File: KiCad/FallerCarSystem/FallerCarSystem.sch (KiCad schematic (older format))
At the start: 32 parts, among them M1 Motor_DC, Q1 BS170F, SW1 SW_DIP_x01, SW2 SW_Reed, U1 PIC12F675-ISN, U2 LT3080xST, U3 MCP1525-TT

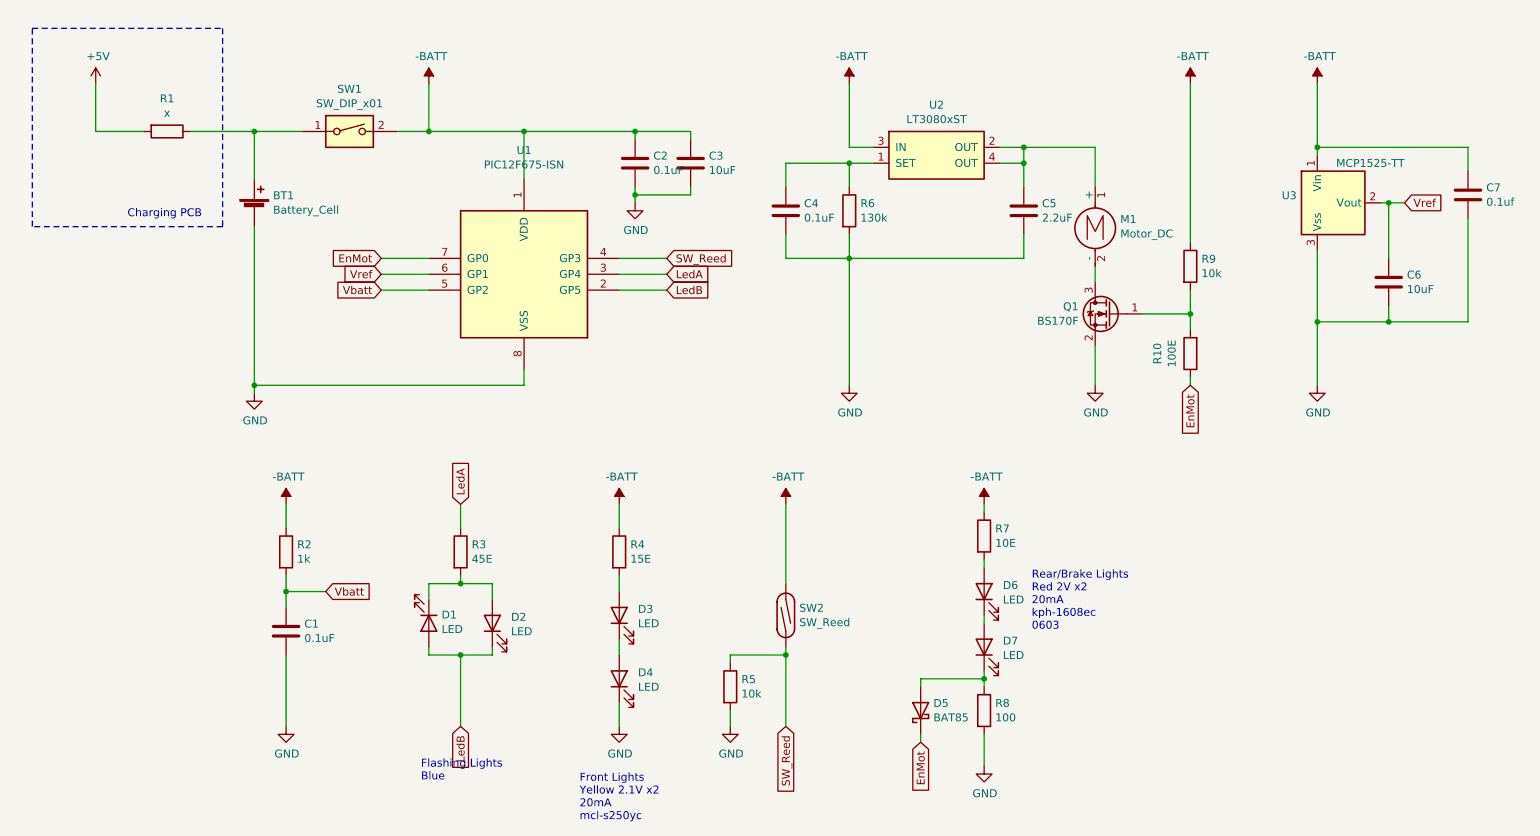
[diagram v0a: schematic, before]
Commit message: jumped to new PIC: 16F-LF-15324. Updated schematic.
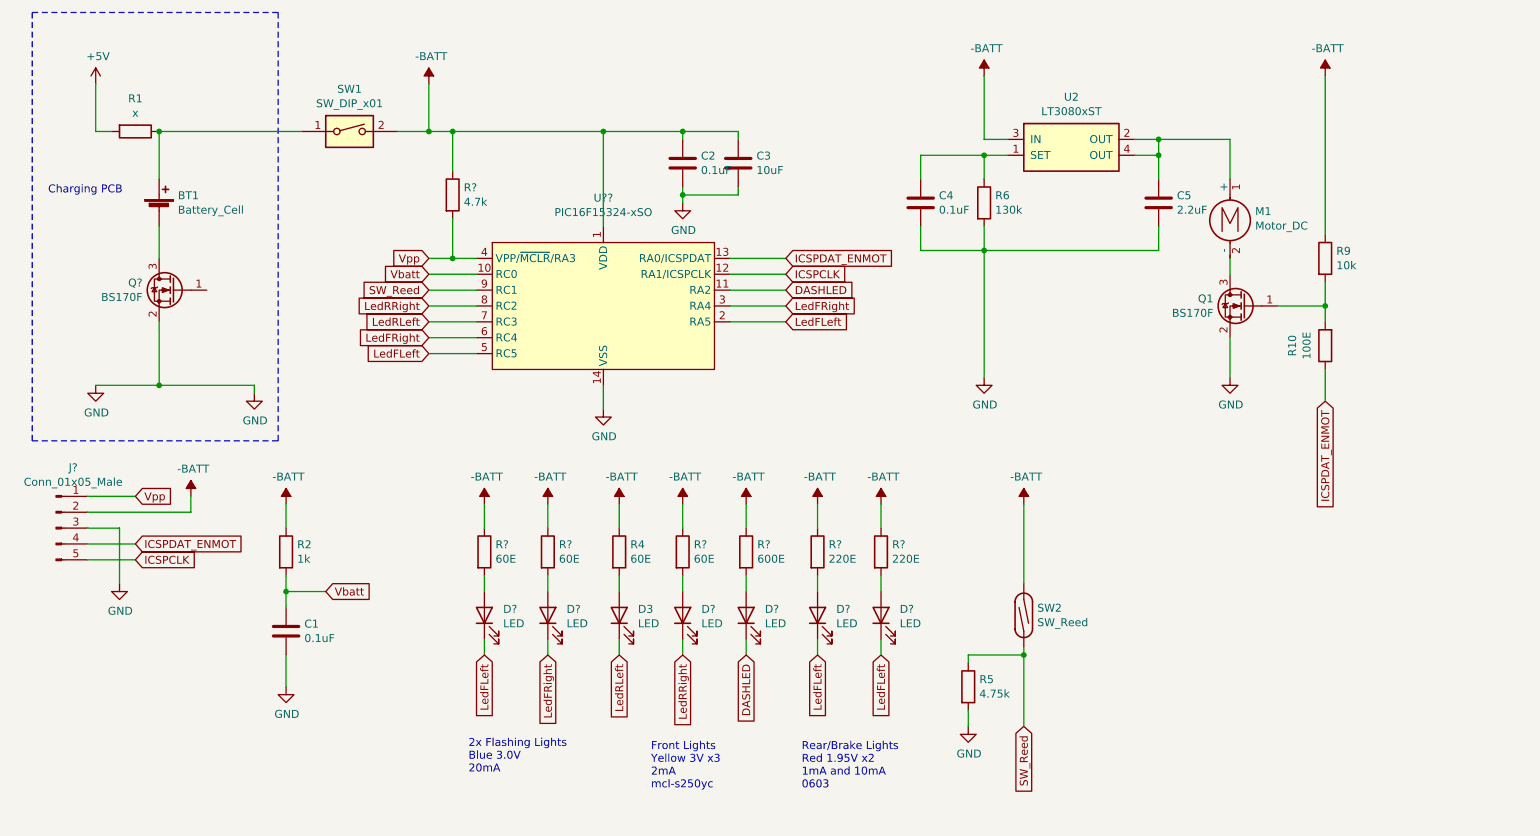
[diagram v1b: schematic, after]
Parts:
- removed C6: 10uF, symbol Device:C
- removed C7: 0.1uf, symbol Device:C
- removed D1, D2, D4, D6, D7: LED, symbol Device:LED
- removed D5: BAT85, Diode_THT:D_DO-35_SOD27_P7.62mm_Horizontal, symbol Diode:BAT85
- removed R3: 45E, symbol Device:R
- removed R7: 10E, symbol Device:R
- removed R8: 100, symbol Device:R
- removed U1: PIC12F675-ISN, Package_DIP:DIP-8_W7.62mm, symbol MCU_Microchip_PIC12:PIC12F675-ISN
- removed U3: MCP1525-TT, Package_TO_SOT_SMD:SOT-23, symbol Reference_Voltage:MCP1525-TT
- added D? (x6): LED, symbol Device:LED
- added J?: Conn_01x05_Male, symbol Connector:Conn_01x05_Male
- added Q?: BS170F, Package_TO_SOT_SMD:SOT-23, symbol Transistor_FET:BS170F
- added R?: 4.7k, symbol Device:R
- added R? (x3): 60E, symbol Device:R
- added R?: 600E, symbol Device:R
- added R? (x2): 220E, symbol Device:R
- added U??: PIC16F15324-xSO, Package_SO:SOIC-14W_7.5x17.9mm_P1.27mm, symbol MCU_Microchip_PIC16:PIC16F15324-xSO
- R4: value 15E -> 60E
- R5: value 10k -> 4.75k
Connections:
- net -BATT: now also J?.2 (Pin_2), R?.1, R?.1, R?.1, R?.1, R?.1, R?.1, R?.1, U??.1 (VDD)
- net GND: now also J?.3 (Pin_3), Q?.2 (S), U??.14 (VSS); no longer BT1.2 (-)
- net SW_Reed: now also U??.9 (RC1)
- net Vbatt: now also U??.10 (RC0)
- net LedRLeft: now reaches D3.1 (K)
- net LedRLeft: now also U??.7 (RC3)
- net EnMot renamed ICSPDAT_ENMOT
- net ICSPDAT_ENMOT: now also J?.4 (Pin_4), U??.13 (RA0/ICSPDAT)
- new net: BT1.2 (-), Q?.3 (D)
- new net: D?.2 (A), R?.2 (x6)
- new net DASHLED: D?.1 (K), U??.11 (RA2)
- new net ICSPCLK: J?.5 (Pin_5), U??.12 (RA1/ICSPCLK)
- new net LedFLeft: D?.1 (K), D?.1 (K), D?.1 (K), U??.2 (RA5), U??.5 (RC5)
- new net LedFRight: D?.1 (K), U??.3 (RA4), U??.6 (RC4)
- new net LedRRight: D?.1 (K), U??.8 (RC2)
- new net Vpp: J?.1 (Pin_1), R?.2, U??.4 (VPP/~MCLR~/RA3)
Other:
- note added: "2x Flashing Lights\nBlue 3.0V\n20mA"
- note added: "Front Lights\nYellow 3V x3\n2mA\nmcl-s250yc"
- note added: "Rear/Brake Lights\nRed 1.95V x2\n1mA and 10mA\n0603"
- note removed: "Flashing Lights\nBlue"
- note removed: "Front Lights\nYellow 2.1V x2\n20mA\nmcl-s250yc"
- note removed: "Rear/Brake Lights\nRed 2V x2\n20mA\nkph-1608ec\n0603"
- moved on the sheet: BT1, C2, C3, C4, C5, M1, Q1, R1, R10, R5, R6, R9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

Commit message: First proto version faller car system done. To do: - develop PCB with charger on it etc - Front led lights in flash mode may go deeper off
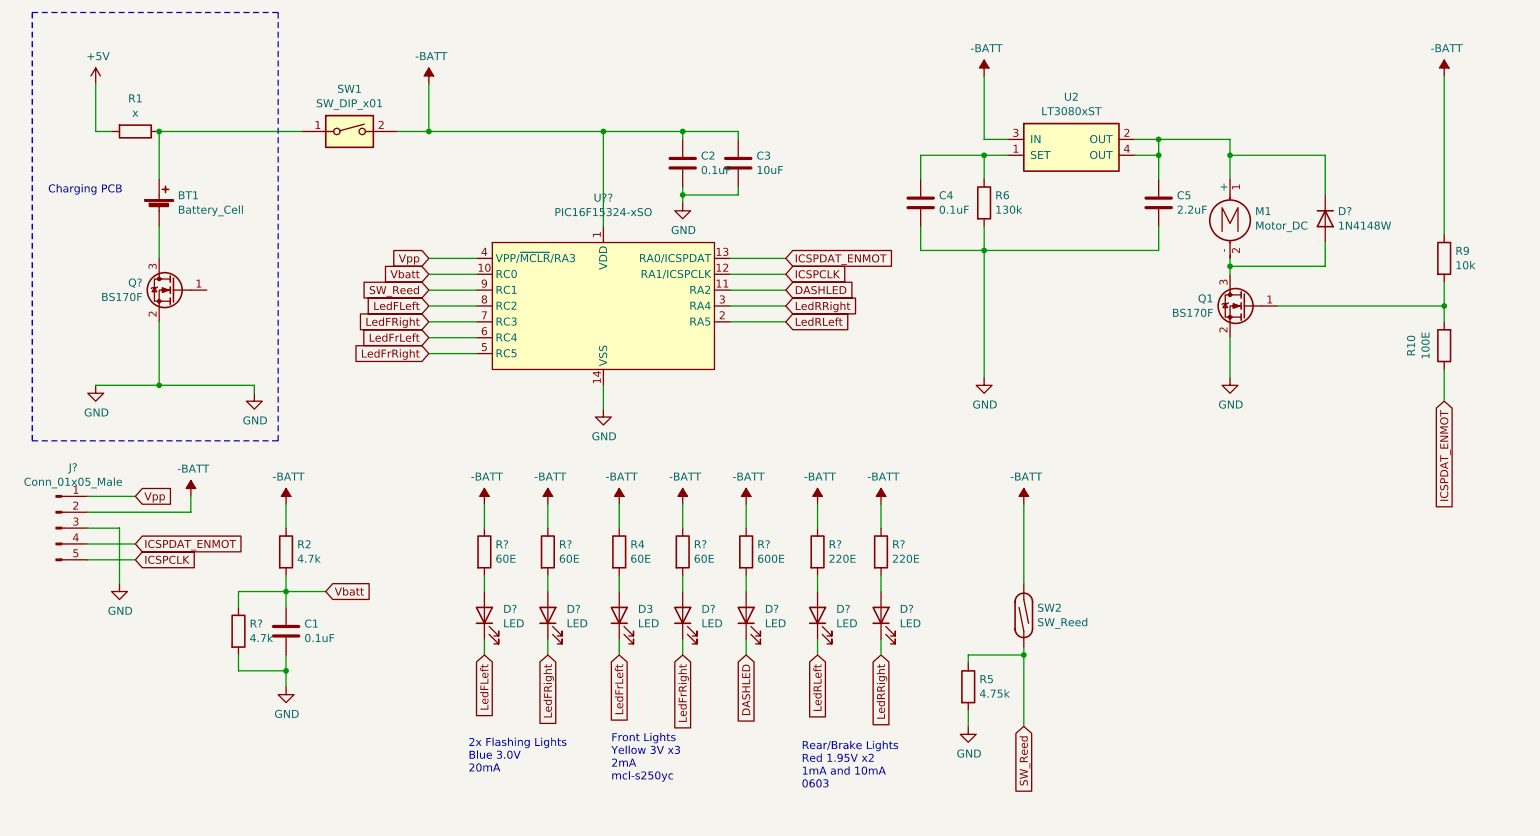
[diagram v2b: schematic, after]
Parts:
- removed R?: 4.7k, symbol Device:R
- added D?: 1N4148W, Diode_SMD:D_SOD-123, symbol Diode:1N4148W
- added R?: 4.7k, symbol Device:R
- R2: value 1k -> 4.7k
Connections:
- net GND: now also R?.2
- net LedFLeft: now also U??.8 (RC2); no longer D?.1 (K), D?.1 (K), U??.2 (RA5), U??.5 (RC5)
- net LedFRight: now also U??.7 (RC3); no longer U??.3 (RA4), U??.6 (RC4)
- net LedRLeft: now also D?.1 (K), U??.2 (RA5); no longer D3.1 (K), U??.7 (RC3)
- net LedRRight: now also D?.1 (K), U??.3 (RA4); no longer D?.1 (K), U??.8 (RC2)
- net Vbatt: now also R?.1
- net at C5.1, M1.1 (+), U2.2 (OUT)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: now also D?.1 (K)
- net at M1.2 (-), Q1.3 (D): now also D?.2 (A)
- new net LedFrLeft: D3.1 (K), U??.6 (RC4)
- new net LedFrRight: D?.1 (K), U??.5 (RC5)
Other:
- moved on the sheet: R10, R9
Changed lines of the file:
@@
 P 2400 4150
 F 0 "R2" H 2470 4196 50  0000 L CNN
-F 1 "1k" H 2470 4105 50  0000 L CNN
+F 1 "4.7k" H 2470 4105 50  0000 L CNN
 F 2 "" V 2330 4150 50  0001 C CNN
 F 3 "~" H 2400 4150 50  0001 C CNN
@@
 L Device:R R10
 U 1 1 639E8742
-P 8950 2850
-F 0 "R10" V 9157 2850 50  0000 C CNN
-F 1 "100E" V 9066 2850 50  0000 C CNN
-F 2 "" V 8880 2850 50  0001 C CNN
-F 3 "~" H 8950 2850 50  0001 C CNN
-	1    8950 2850
+P 9700 2850
+F 0 "R10" V 9907 2850 50  0000 C CNN
+F 1 "100E" V 9816 2850 50  0000 C CNN
+F 2 "" V 9630 2850 50  0001 C CNN
+F 3 "~" H 9700 2850 50  0001 C CNN
+	1    9700 2850
 	-1   0    0    1
 $EndComp
@@
 L Device:R R9
 U 1 1 639EBB86
-P 8950 2300
-F 0 "R9" H 9020 2346 50  0000 L CNN
-F 1 "10k" H 9020 2255 50  0000 L CNN
-F 2 "" V 8880 2300 50  0001 C CNN
-F 3 "~" H 8950 2300 50  0001 C CNN
-	1    8950 2300
+P 9700 2300
+F 0 "R9" H 9770 2346 50  0000 L CNN
+F 1 "10k" H 9770 2255 50  0000 L CNN
+F 2 "" V 9630 2300 50  0001 C CNN
+F 3 "~" H 9700 2300 50  0001 C CNN
+	1    9700 2300
 	1    0    0    -1
 $EndComp
@@
 Wire Wire Line
 	4500 4300 4500 4400
-Text Notes 4700 5650 0    50   ~ 0
-Front Lights\nYellow 3V x3\n2mA\nmcl-s250yc
 Wire Wire Line
 	6800 1550 6950 1550
@@
 Connection ~ 7900 1550
 Wire Wire Line
-	8350 2400 8350 2300
-Wire Wire Line
-	8350 1800 8350 1550
+	8350 2400 8350 2350
+Wire Wire Line
+	8350 1800 8350 1650
 $Comp
 L power:-BATT #PWR010
@@
 L power:-BATT #PWR016
 U 1 1 63ADE5C4
-P 8950 1150
-F 0 "#PWR016" H 8950 1000 50  0001 C CNN
-F 1 "-BATT" H 8965 1323 50  0000 C CNN
-F 2 "" H 8950 1150 50  0001 C CNN
-F 3 "" H 8950 1150 50  0001 C CNN
-	1    8950 1150
-	1    0    0    -1
-$EndComp
-Wire Wire Line
-	8950 1150 8950 2150
-Wire Wire Line
-	8950 2450 8950 2600
-Wire Wire Line
-	8950 2600 8650 2600
-Wire Wire Line
-	8950 2600 8950 2700
-Connection ~ 8950 2600
+P 9700 1150
+F 0 "#PWR016" H 9700 1000 50  0001 C CNN
+F 1 "-BATT" H 9715 1323 50  0000 C CNN
+F 2 "" H 9700 1150 50  0001 C CNN
+F 3 "" H 9700 1150 50  0001 C CNN
+	1    9700 1150
+	1    0    0    -1
+$EndComp
+Wire Wire Line
+	9700 1150 9700 2150
+Wire Wire Line
+	9700 2450 9700 2600
+Wire Wire Line
+	9700 2600 9700 2700
+Connection ~ 9700 2600
 Wire Wire Line
 	8350 2800 8350 3050
@@
 	1    0    0    -1
 $EndComp
-Wire Wire Line
-	3300 1500 3450 1500
 Connection ~ 3300 1500
 Wire Wire Line
@@
 Text GLabel 3300 2300 0    50   Input ~ 0
 Vpp
-Wire Wire Line
-	3300 2300 3450 2300
-$Comp
-L Device:R R?
-U 1 1 63A04FA2
-P 3450 1900
-F 0 "R?" H 3520 1946 50  0000 L CNN
-F 1 "4.7k" H 3520 1855 50  0000 L CNN
-F 2 "" V 3380 1900 50  0001 C CNN
-F 3 "~" H 3450 1900 50  0001 C CNN
-	1    3450 1900
-	1    0    0    -1
-$EndComp
-Wire Wire Line
-	3450 2050 3450 2300
-Connection ~ 3450 2300
-Wire Wire Line
-	3450 2300 3600 2300
-Wire Wire Line
-	3450 1500 3450 1750
-Connection ~ 3450 1500
-Wire Wire Line
-	3450 1500 4400 1500
 Text GLabel 1450 3800 2    50   Input ~ 0
 Vpp
@@
 Wire Wire Line
 	4400 3250 4400 3100
-Text GLabel 8950 3200 3    50   Input ~ 0
+Text GLabel 9700 3200 3    50   Input ~ 0
 ICSPDAT_ENMOT
 Wire Wire Line
-	8950 3000 8950 3200
+	9700 3000 9700 3200
 Text GLabel 5550 2500 2    50   Input ~ 0
 DASHLED
@@
 Wire Wire Line
 	3300 2500 3600 2500
+Text GLabel 3300 2900 0    50   Input ~ 0
+LedFrRight
+Text GLabel 3300 2800 0    50   Input ~ 0
+LedFrLeft
+Text GLabel 5550 2600 2    50   Input ~ 0
+LedRRight
 Text GLabel 3300 2600 0    50   Input ~ 0
-LedRRight
+LedFLeft
 Text GLabel 3300 2700 0    50   Input ~ 0
-LedRLeft
-Text GLabel 3300 2800 0    50   Input ~ 0
-LedFRight
-Text GLabel 3300 2900 0    50   Input ~ 0
-LedFLeft
-Wire Wire Line
-	3300 2600 3600 2600
-Wire Wire Line
-	3600 2700 3300 2700
-Wire Wire Line
-	3300 2800 3600 2800
-Wire Wire Line
-	3600 2900 3300 2900
-Text GLabel 5550 2600 2    50   Input ~ 0
 LedFRight
 Text GLabel 5550 2700 2    50   Input ~ 0
-LedFLeft
+LedRLeft
 Wire Wire Line
 	5550 2300 5200 2300
@@
 Wire Wire Line
 	5550 2500 5200 2500
-Wire Wire Line
-	5200 2600 5550 2600
-Wire Wire Line
-	5550 2700 5200 2700
 $Comp
 L power:-BATT #PWR?
@@
 Text GLabel 4050 4800 3    50   Input ~ 0
 LedFRight
-Text GLabel 4500 4800 3    50   Input ~ 0
-LedRLeft
-Text GLabel 4900 4800 3    50   Input ~ 0
-LedRRight
-Text GLabel 5750 4800 3    50   Input ~ 0
-LedFLeft
-Text GLabel 6150 4800 3    50   Input ~ 0
-LedFLeft
 Text GLabel 5300 4800 3    50   Input ~ 0
 DASHLED
@@
 	6150 4700 6150 4800
 Wire Wire Line
-	2400 4800 2400 5000
+	2400 4800 2400 4900
 Wire Wire Line
 	1350 4350 1350 4000
 Wire Wire Line
 	1350 4000 1150 4000
+$Comp
+L Device:R R?
+U 1 1 639DE365
+P 2100 4650
+F 0 "R?" H 2170 4696 50  0000 L CNN
+F 1 "4.7k" H 2170 4605 50  0000 L CNN
+F 2 "" V 2030 4650 50  0001 C CNN
+F 3 "~" H 2100 4650 50  0001 C CNN
+	1    2100 4650
+	1    0    0    -1
+$EndComp
+Wire Wire Line
+	2100 4500 2100 4400
+Wire Wire Line
+	2100 4400 2400 4400
+Wire Wire Line
+	2400 4900 2100 4900
+Wire Wire Line
+	2100 4900 2100 4800
+Connection ~ 2400 4900
+Wire Wire Line
+	2400 4900 2400 5000
+Wire Wire Line
+	3600 2600 3300 2600
+Wire Wire Line
+	3300 2700 3600 2700
+Wire Wire Line
+	3600 2800 3300 2800
+Wire Wire Line
+	3300 2900 3600 2900
+Wire Wire Line
+	5550 2600 5200 2600
+Wire Wire Line
+	5550 2700 5200 2700
+Wire Wire Line
+	3300 1500 4400 1500
+Wire Wire Line
+	3300 2300 3600 2300
+Text Notes 4450 5600 0    50   ~ 0
+Front Lights\nYellow 3V x3\n2mA\nmcl-s250yc
+Text GLabel 5750 4800 3    50   Input ~ 0
+LedRLeft
+Text GLabel 6150 4800 3    50   Input ~ 0
+LedRRight
+Text GLabel 4900 4800 3    50   Input ~ 0
+LedFrRight
+Text GLabel 4500 4800 3    50   Input ~ 0
+LedFrLeft
+$Comp
+L Diode:1N4148W D?
+U 1 1 63A3C7A6
+P 8950 2050
+F 0 "D?" V 8904 2130 50  0000 L CNN
+F 1 "1N4148W" V 8995 2130 50  0000 L CNN
+F 2 "Diode_SMD:D_SOD-123" H 8950 1875 50  0001 C CNN
+F 3 "https://www.vishay.com/docs/85748/1n4148w.pdf" H 8950 2050 50  0001 C CNN
+	1    8950 2050
+	0    1    1    0
+$EndComp
+Wire Wire Line
+	8650 2600 9700 2600
+Wire Wire Line
+	8950 1900 8950 1650
+Wire Wire Line
+	8950 1650 8350 1650
+Connection ~ 8350 1650
+Wire Wire Line
+	8350 1650 8350 1550
+Wire Wire Line
+	8950 2200 8950 2350
+Wire Wire Line
+	8950 2350 8350 2350
+Connection ~ 8350 2350
+Wire Wire Line
+	8350 2350 8350 2300
 $EndSCHEMATC
